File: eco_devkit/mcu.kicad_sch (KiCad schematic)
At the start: 46 parts, among them J1 USB_C_Receptacle_USB2.0_16P, J2 GPIO1, J3 Conn_01x20, SW1 BOOT, SW2 RESET, Y1 Crystal_GND24

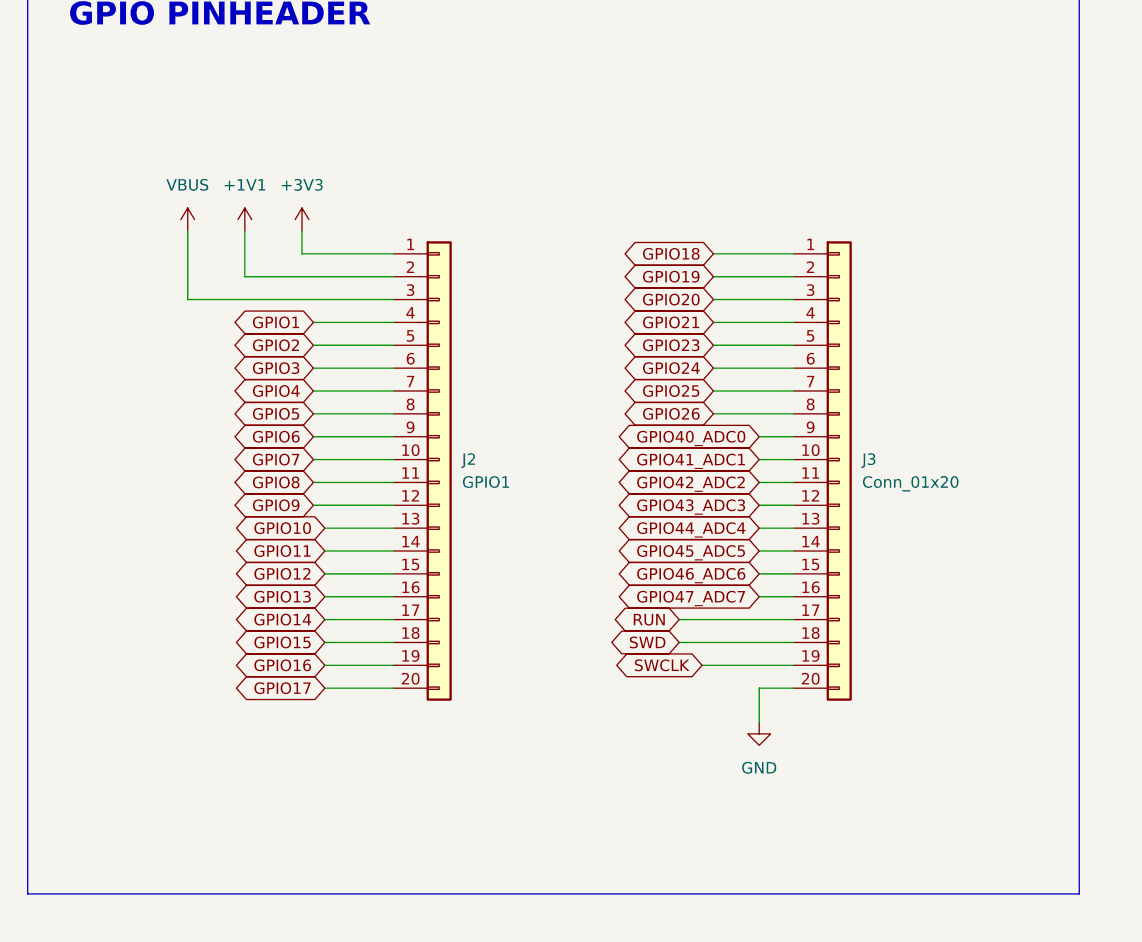
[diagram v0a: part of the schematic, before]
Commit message: Corrige footprints.
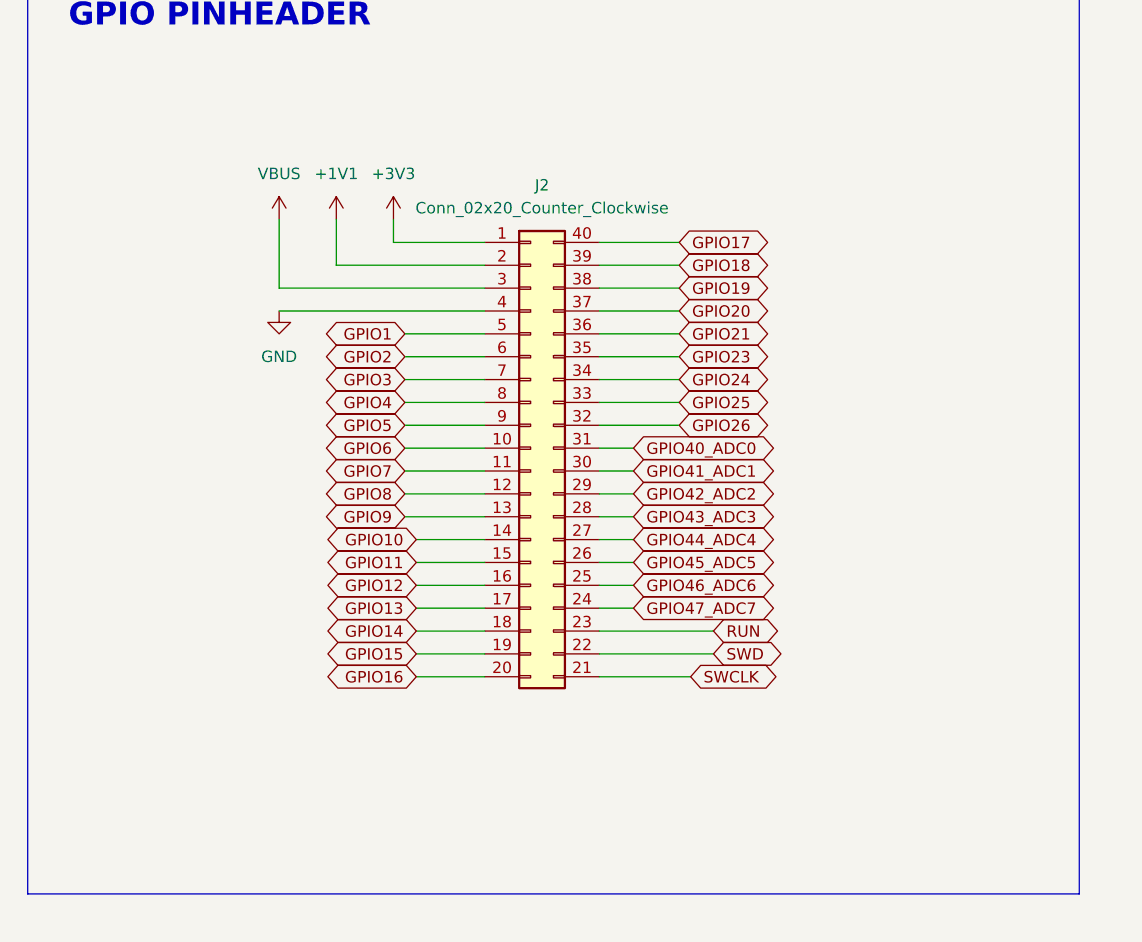
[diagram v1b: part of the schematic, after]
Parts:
- removed J2: GPIO1, Connector_PinHeader_2.54mm:PinHeader_1x20_P2.54mm_Vertical, symbol Connector_Generic:Conn_01x20
- removed J3: Conn_01x20, Connector_PinHeader_2.54mm:PinHeader_1x20_P2.54mm_Vertical, symbol Connector_Generic:Conn_01x20
- added J2: Conn_02x20_Counter_Clockwise, Connector_PinHeader_2.54mm:PinHeader_2x20_P2.54mm_Vertical, symbol Connector_Generic:Conn_02x20_Counter_Clockwise
- D1: footprint Diode_THT:D_DO-41_SOD81_P10.16mm_Horizontal -> Diode_SMD:D_SOD-123F
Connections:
- net +1V1: now also J2.2 (Pin_2)
- net +3V3: now also J2.1 (Pin_1)
- net ACCEL_MISO: now also J2.37 (Pin_37)
- net ACCEL_MOSI: now also J2.38 (Pin_38)
- net ACCEL_SCK: now also J2.39 (Pin_39)
- net DISPLAY_EN: now also J2.17 (Pin_17)
- net DISPLAY_MOSI: now also J2.15 (Pin_15)
- net DISPLAY_RST: now also J2.16 (Pin_16)
- net DISPLAY_SCK: now also J2.14 (Pin_14)
- net GND: now also J2.4 (Pin_4)
- net GPIO1: now also J2.5 (Pin_5)
- net GPIO14: now also J2.18 (Pin_18)
- net GPIO15: now also J2.19 (Pin_19)
- net GPIO16: now also J2.20 (Pin_20)
- net GPIO17: now also J2.40 (Pin_40)
- net GPIO2: now also J2.6 (Pin_6)
- net GPIO21: now also J2.36 (Pin_36)
- net GPIO23: now also J2.35 (Pin_35)
- net GPIO24: now also J2.34 (Pin_34)
- net GPIO25: now also J2.33 (Pin_33)
- net GPIO26: now also J2.32 (Pin_32)
- net GPIO3: now also J2.7 (Pin_7)
- net GPIO4: now also J2.8 (Pin_8)
- net GPIO40_ADC0: now also J2.31 (Pin_31)
- net GPIO41_ADC1: now also J2.30 (Pin_30)
- net GPIO42_ADC2: now also J2.29 (Pin_29)
- net GPIO43_ADC3: now also J2.24 (Pin_24), J2.28 (Pin_28)
- net GPIO44_ADC4: now also J2.27 (Pin_27)
- net GPIO45_ADC5: now also J2.26 (Pin_26)
- net GPIO46_ADC6: now also J2.25 (Pin_25)
- net GPIO5: now also J2.9 (Pin_9)
- net GPIO6: now also J2.10 (Pin_10)
- net GPIO7: now also J2.11 (Pin_11)
- net GPIO8: now also J2.12 (Pin_12)
- net GPIO9: now also J2.13 (Pin_13)
- net RUN: now also J2.23 (Pin_23)
- net SWCLK: now also J2.21 (Pin_21)
- net SWD: now also J2.22 (Pin_22)
- net VBUS: now also J2.3 (Pin_3)

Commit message: refining adjustments on RP2350 and it's modules
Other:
- note added: "MCU RP2350"
- moved on the sheet: C1, C10, C11, C12, C13, C14, C15, C16, C17, C18, C19, C2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

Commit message: changing global labels to local
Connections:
- net GPIO23: now also RP2350B1.23 (GPIO23)
- net SWD: no longer RP2350B1.34 (SWDIO)
- net XIN: no longer RP2350B1.30 (XIN)
- net XOUT: now also RP2350B1.30 (XIN)
- new net SWDIO: RP2350B1.34 (SWDIO)

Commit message: footprint completed
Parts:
- C1, C2: MPN (none) -> C0603C150K8RACAUTO
- R1: value DNF -> 0
- R5: value DNF -> 10k
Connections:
- net VBUS is gone; now on net +VBUS: J2.3 (Pin_3)
- net QSPI_SS: now also R9.2, RP2350B1.75 (QSPI_SS)
- net RUN: now also RP2350B1.35 (RUN), SW2.2
- net GPIO0 renamed PROBE_GPIO4/UART_TX
- net GPIO1 renamed POBRE_GPIO5/UART_RX
- net GPIO26 renamed PIN_BUZZER
- net GPIO30 renamed GPIO_MOSFET_GATE_IN
- net GPIO31 renamed PIN_LED_RED
- net GPIO32 renamed PIN_LED_GREEN
- net GPIO33 renamed PIN_LED_BLUE
- net GPIO34 renamed PIN_LED_YELLOW
- net GPIO35 renamed PIN_ADDRESSABE
- net GPIO36 renamed PIN_BTN1
- net GPIO37 renamed PIN_BTN2
- net GPIO38 renamed PIN_BTN3
- net GPIO39 renamed PIN_BTN4
- net GPIO4 renamed PIN_LIGHT_SENS_SDA
- net GPIO5 renamed PIN_LIGHT_SENS_SCL
- net GPIO7 renamed PIN_WIFI_RESET_BL
- net GPIO8 renamed PIN_WIFI_RX
- net GPIO9 renamed PIN_WIFI_TX
- net SWCLK renamed PROBE_GPIO2/SWCLK
- net SWDIO renamed POBRE_GPIO3/SWDIO
- no-connect marks 3 -> 4
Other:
- moved on the sheet: C5

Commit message: fix:adjustments to component placement and routing
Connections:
- net ACCEL_MISO: now also J2.24 (Pin_24); no longer J2.37 (Pin_37)
- net ACCEL_MOSI: now also J2.23 (Pin_23); no longer J2.38 (Pin_38)
- net ACCEL_SCK: now also J2.22 (Pin_22); no longer J2.39 (Pin_39)
- net GPIO17: now also J2.21 (Pin_21); no longer J2.40 (Pin_40)
- net GPIO21: now also J2.25 (Pin_25); no longer J2.36 (Pin_36)
- net GPIO23: now also J2.26 (Pin_26); no longer J2.35 (Pin_35)
- net GPIO24: now also J2.27 (Pin_27); no longer J2.34 (Pin_34)
- net GPIO25: now also J2.28 (Pin_28); no longer J2.33 (Pin_33)
- net GPIO40_ADC0: now also J2.30 (Pin_30); no longer J2.31 (Pin_31)
- net GPIO41_ADC1: now also J2.31 (Pin_31); no longer J2.30 (Pin_30)
- net GPIO42_ADC2: now also J2.32 (Pin_32); no longer J2.29 (Pin_29)
- net GPIO43_ADC3: now also J2.33 (Pin_33), J2.40 (Pin_40); no longer J2.24 (Pin_24), J2.28 (Pin_28)
- net GPIO44_ADC4: now also J2.34 (Pin_34); no longer J2.27 (Pin_27)
- net GPIO45_ADC5: now also J2.35 (Pin_35); no longer J2.26 (Pin_26)
- net GPIO46_ADC6: now also J2.36 (Pin_36); no longer J2.25 (Pin_25)
- net PIN_BUZZER: now also J2.29 (Pin_29); no longer J2.32 (Pin_32)
- net PROBE_GPIO2/SWCLK: now also J2.37 (Pin_37); no longer J2.21 (Pin_21)
- net RUN: now also J2.39 (Pin_39); no longer J2.23 (Pin_23)
- net SWD: now also J2.38 (Pin_38); no longer J2.22 (Pin_22)
- net XIN: now also RP2350B1.30 (XIN)
- net XOUT: no longer RP2350B1.30 (XIN)

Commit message: Update layout
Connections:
- net GPIO14 renamed DISPLAY_CS
- net GPIO16 renamed IR_RX
- net GPIO17 renamed IR_TX
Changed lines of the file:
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@@
 	(wire
 		(pts
+			(xy 472.44 185.42) (xy 491.49 185.42)
+		)
+		(stroke
+			(width 0)
+			(type default)
+		)
+	)
+	(wire
+		(pts
 			(xy 361.95 161.29) (xy 361.95 130.81)
 		)
@@
 	(wire
 		(pts
-			(xy 393.7 215.9) (xy 386.08 215.9)
+			(xy 386.08 215.9) (xy 403.86 215.9)
 		)
 		(stroke
@@
 	(wire
 		(pts
-			(xy 393.7 218.44) (xy 386.08 218.44)
+			(xy 386.08 218.44) (xy 403.86 218.44)
 		)
 		(stroke
@@
 		)
 	)
+	(global_label "IR_TX"
+		(shape output)
+		(at 403.86 218.44 0)
+		(fields_autoplaced yes)
+		(effects
+			(font
+				(size 1.27 1.27)
+				(thickness 0.1588)
+			)
+			(justify left)
+		)
+		(property "Intersheetrefs" "${INTERSHEET_REFS}"
+			(at 411.8647 218.44 0)
+			(effects
+				(font
+					(size 1.27 1.27)
+				)
+				(justify left)
+				(hide yes)
+			)
+		)
+	)
 	(global_label "GPIO41_ADC1"
 		(shape bidirectional)
@@
 		)
 	)
+	(global_label "GPIO14"
+		(shape bidirectional)
+		(at 472.44 185.42 180)
+		(fields_autoplaced yes)
+		(effects
+			(font
+				(size 1.27 1.27)
+			)
+			(justify right)
+		)
+		(property "Intersheetrefs" "${INTERSHEET_REFS}"
+			(at 461.4492 185.42 0)
+			(effects
+				(font
+					(size 1.27 1.27)
+				)
+				(justify right)
+				(hide yes)
+			)
+		)
+	)
 	(global_label "GPIO13"
 		(shape bidirectional)
@@
 		)
 	)
+	(global_label "DISPLAY_CS"
+		(shape output)
+		(at 491.49 185.42 0)
+		(fields_autoplaced yes)
+		(effects
+			(font
+				(size 1.27 1.27)
+			)
+			(justify left)
+		)
+		(property "Intersheetrefs" "${INTERSHEET_REFS}"
+			(at 505.4819 185.42 0)
+			(effects
+				(font
+					(size 1.27 1.27)
+				)
+				(justify left)
+				(hide yes)
+			)
+		)
+	)
 	(global_label "GPIO47_ADC7"
 		(shape bidirectional)
@@
 				(hide yes)
 			)
+		)
+	)
+	(global_label "IR_RX"
+		(shape output)
+		(at 403.86 215.9 0)
+		(fields_autoplaced yes)
+		(effects
+			(font
+				(size 1.27 1.27)
+				(thickness 0.1588)
+			)
+			(justify left)
+		)
+		(property "Intersheetrefs" "${INTERSHEET_REFS}"
+			(at 412.1671 215.9 0)
+			(effects
+				(font
+					(size 1.27 1.27)
+				)
+				(justify left)
+				(hide yes)
+			)

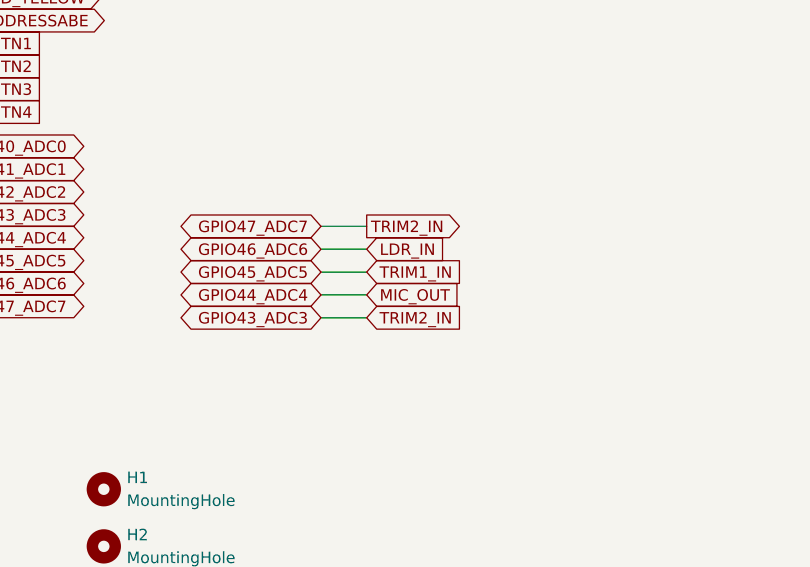
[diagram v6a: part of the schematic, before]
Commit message: Add all nets
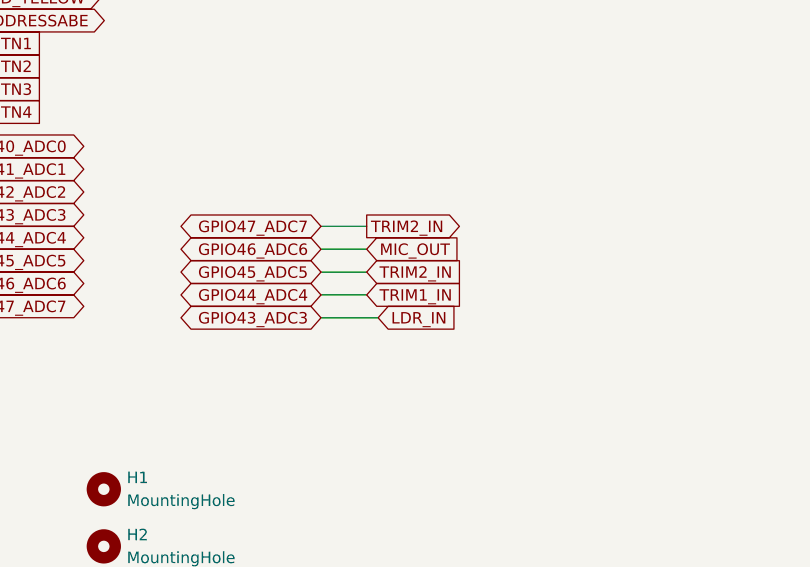
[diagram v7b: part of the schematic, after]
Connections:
- net GPIO43_ADC3: no longer J2.40 (Pin_40), RP2350B1.58 (GPIO47_ADC7)
- net GPIO45_ADC5: now also J2.40 (Pin_40), RP2350B1.58 (GPIO47_ADC7)
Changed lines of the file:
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@@
 	(wire
 		(pts
-			(xy 445.77 289.56) (xy 440.69 289.56)
-		)
-		(stroke
-			(width 0)
-			(type default)
-		)
-	)
-	(wire
-		(pts
 			(xy 474.98 110.49) (xy 474.98 114.3)
 		)
@@
 	(wire
 		(pts
+			(xy 440.69 292.1) (xy 445.77 292.1)
+		)
+		(stroke
+			(width 0)
+			(type default)
+		)
+	)
+	(wire
+		(pts
 			(xy 255.27 158.75) (xy 255.27 170.18)
 		)
@@
 	(wire
 		(pts
-			(xy 445.77 294.64) (xy 440.69 294.64)
-		)
-		(stroke
-			(width 0)
-			(type default)
-		)
-	)
-	(wire
-		(pts
 			(xy 386.08 261.62) (xy 398.78 261.62)
 		)
@@
 	(wire
 		(pts
-			(xy 445.77 292.1) (xy 440.69 292.1)
-		)
-		(stroke
-			(width 0)
-			(type default)
-		)
-	)
-	(wire
-		(pts
 			(xy 393.7 226.06) (xy 386.08 226.06)
 		)
@@
 	(wire
 		(pts
+			(xy 440.69 294.64) (xy 445.77 294.64)
+		)
+		(stroke
+			(width 0)
+			(type default)
+		)
+	)
+	(wire
+		(pts
 			(xy 255.27 146.05) (xy 255.27 151.13)
 		)
@@
 	(wire
 		(pts
+			(xy 440.69 297.18) (xy 447.04 297.18)
+		)
+		(stroke
+			(width 0)
+			(type default)
+		)
+	)
+	(wire
+		(pts
 			(xy 459.74 102.87) (xy 459.74 105.41)
 		)
@@
 	(wire
 		(pts
-			(xy 445.77 297.18) (xy 440.69 297.18)
-		)
-		(stroke
-			(width 0)
-			(type default)
-		)
-	)
-	(wire
-		(pts
 			(xy 316.23 101.6) (xy 326.39 101.6)
 		)
@@
 	(wire
 		(pts
+			(xy 440.69 289.56) (xy 445.77 289.56)
+		)
+		(stroke
+			(width 0)
+			(type default)
+		)
+	)
+	(wire
+		(pts
 			(xy 403.86 160.02) (xy 417.83 160.02)
 		)
@@
 	(global_label "LDR_IN"
 		(shape input)
-		(at 445.77 289.56 0)
+		(at 447.04 297.18 0)
 		(fields_autoplaced yes)
 		(effects
@@
 		)
 		(property "Intersheetrefs" "${INTERSHEET_REFS}"
-			(at 455.2262 289.56 0)
+			(at 456.4962 297.18 0)
 			(effects
 				(font
@@
 	(global_label "MIC_OUT"
 		(shape input)
-		(at 445.77 294.64 0)
+		(at 445.77 289.56 0)
 		(fields_autoplaced yes)
 		(effects
@@
 		)
 		(property "Intersheetrefs" "${INTERSHEET_REFS}"
-			(at 456.6776 294.64 0)
+			(at 456.6776 289.56 0)
 			(effects
 				(font
@@
 	(global_label "TRIM1_IN"
 		(shape input)
-		(at 445.77 292.1 0)
+		(at 445.77 294.64 0)
 		(fields_autoplaced yes)
 		(effects
@@
 		)
 		(property "Intersheetrefs" "${INTERSHEET_REFS}"
-			(at 457.1614 292.1 0)
+			(at 457.1614 294.64 0)
 			(effects
 				(font
@@
 	(global_label "TRIM2_IN"
 		(shape input)
-		(at 445.77 297.18 0)
+		(at 445.77 292.1 0)
 		(fields_autoplaced yes)
 		(effects
@@
 		)
 		(property "Intersheetrefs" "${INTERSHEET_REFS}"
-			(at 457.1614 297.18 0)
+			(at 457.1614 292.1 0)
 			(effects
 				(font

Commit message: Finish
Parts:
- H1, H2, H3, H4: footprint (none) -> MountingHole:MountingHole_2.7mm_Pad_Via
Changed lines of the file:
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@@
 			)
 		)
-		(property "Footprint" ""
+		(property "Footprint" "MountingHole:MountingHole_2.7mm_Pad_Via"
 			(at 416.56 335.28 0)
 			(effects
@@
 			)
 		)
-		(property "Footprint" ""
+		(property "Footprint" "MountingHole:MountingHole_2.7mm_Pad_Via"
 			(at 416.56 328.93 0)
 			(effects
@@
 			)
 		)
-		(property "Footprint" ""
+		(property "Footprint" "MountingHole:MountingHole_2.7mm_Pad_Via"
 			(at 416.56 316.23 0)
 			(effects
@@
 			)
 		)
-		(property "Footprint" ""
+		(property "Footprint" "MountingHole:MountingHole_2.7mm_Pad_Via"
 			(at 416.56 322.58 0)
 			(effects
